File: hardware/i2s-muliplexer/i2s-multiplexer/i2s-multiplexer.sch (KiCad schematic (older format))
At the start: 18 parts, among them J1 Conn_01x07, J10 Conn_01x04, J2 Conn_01x04, J3 Conn_01x04, J4 Conn_01x04, J5 Conn_01x04, J6 Conn_01x04, J7 Conn_01x04, J8 Conn_01x04, J9 Conn_01x04, U1 74HC4051, U2 74HC4051, U3 74HC4051, U4 74HC4051, U5 74HC126

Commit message: Using buffers
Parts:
- removed J2, J7, J8, J9: Conn_01x04, Connector_PinHeader_2.54mm:PinHeader_1x04_P2.54mm_Vertical, symbol Connector_Generic:Conn_01x04
- removed U1, U2, U3, U4: 74HC4051, Package_SO:SOIC-16_3.9x9.9mm_P1.27mm, symbol 74xx:74HC4051
- removed U5: 74HC126, Package_SO:SOIC-14_3.9x8.7mm_P1.27mm, symbol 74xx:74LS126
- added J4: Conn_01x04, Connector_PinHeader_2.54mm:PinHeader_1x04_P2.54mm_Vertical, symbol Connector_Generic:Conn_01x04
- added R4, R6: 10K, symbol Device:R_Small
- added R5: R_Small, symbol Device:R_Small
- added U1, U2, U3, U4, U5, U6: 74HC126, symbol i2s-multiplexer:74HC126
- added U7: 74LS138, symbol 74xx:74LS138
- R1, R2, R3: footprint Resistor_SMD:R_0805_2012Metric_Pad1.15x1.40mm_HandSolder -> (none)
- renumbered J5 to J1, J4 to J2, J6 to J3, J3 to J5, J1 to J6, J10 to J7
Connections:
- net labels added: +3V3, CH_EN_0, CH_EN_1, CH_EN_2, CH_EN_3, CH_EN_4, SRC_EN
- net labels removed: BCLK_5, BCLK_6, BCLK_7, DATA_5, DATA_6, DATA_7, LRCLK_5, LRCLK_6, LRCLK_7, MCLK_5, MCLK_6, MCLK_7, ~SRC_EN
- wire segments 114 -> 172
- no-connect marks 0 -> 3
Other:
- note added: "BCLK"
- note added: "CD"
- note added: "CD\n"
- note added: "DAB \nRadio\n"
- note added: "DATA"
- note added: "LRCLK"
- note added: "MCLK_OUT"
- note added: "Media\nCenter\n"
- note added: "Record\nPlayer\n"
- note added: "SPDIF\nBlueray"
- note removed: "I2S Source Inputs\n"
- moved on the sheet: J6

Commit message: Initial PCB design
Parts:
- removed J7: Conn_01x04, Connector_PinHeader_2.54mm:PinHeader_1x04_P2.54mm_Vertical, symbol Connector_Generic:Conn_01x04
- added J7: Conn_01x05, Connector_PinHeader_2.54mm:PinHeader_1x05_P2.54mm_Vertical, symbol Connector_Generic:Conn_01x05
- J1, J2, J3, J4, J5: value Conn_01x04 -> Conn_01x05; footprint Connector_PinHeader_2.54mm:PinHeader_1x04_P2.54mm_Vertical -> Connector_PinHeader_2.54mm:PinHeader_1x05_P2.54mm_Vertical; symbol Connector_Generic:Conn_01x04 -> Connector_Generic:Conn_01x05
- R1, R2, R3, R4, R6: footprint (none) -> Resistor_SMD:R_0805_2012Metric_Pad1.15x1.40mm_HandSolder
- R5: value R_Small -> 10K; footprint (none) -> Resistor_SMD:R_0805_2012Metric_Pad1.15x1.40mm_HandSolder
- U1, U2, U3, U4, U5, U6: footprint (none) -> Package_SO:SOIC-14_3.9x8.7mm_P1.27mm
- U7: footprint (none) -> Package_SO:SOIC-16_3.9x9.9mm_P1.27mm
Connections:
- net labels added: BCLK_OUT, DATA_OUT, LRCLK_OUT, MCLK_OUT
- wire segments 172 -> 179
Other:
- note removed: "BCLK"
- note removed: "DATA"
- note removed: "LRCLK"
- note removed: "MCLK_OUT"
- moved on the sheet: R1, R2, R3, R4

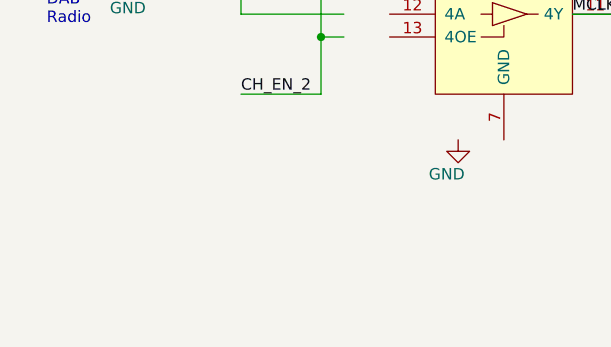
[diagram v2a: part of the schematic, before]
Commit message: Added test point
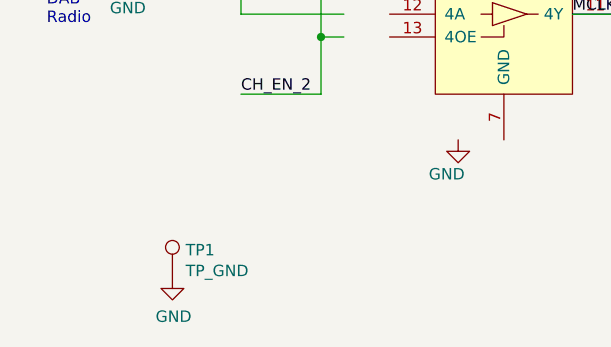
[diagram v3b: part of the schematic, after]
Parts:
- added TP1: TP_GND, Connector_PinHeader_2.54mm:PinHeader_1x01_P2.54mm_Vertical, symbol Connector:TestPoint
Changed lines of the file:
@@
 Text Label 10050 4800 0    50   ~ 0
 LRCLK_OUT
+$Comp
+L Connector:TestPoint TP1
+U 1 1 621031E6
+P 1400 7450
+F 0 "TP1" H 1458 7568 50  0000 L CNN
+F 1 "TP_GND" H 1458 7477 50  0000 L CNN
+F 2 "Connector_PinHeader_2.54mm:PinHeader_1x01_P2.54mm_Vertical" H 1600 7450 50  0001 C CNN
+F 3 "~" H 1600 7450 50  0001 C CNN
+	1    1400 7450
+	1    0    0    -1
+$EndComp
+$Comp
+L power:GND #PWR0105
+U 1 1 6210419F
+P 1400 7450
+F 0 "#PWR0105" H 1400 7200 50  0001 C CNN
+F 1 "GND" H 1405 7277 50  0000 C CNN
+F 2 "" H 1400 7450 50  0001 C CNN
+F 3 "" H 1400 7450 50  0001 C CNN
+	1    1400 7450
+	1    0    0    -1
+$EndComp
 $EndSCHEMATC

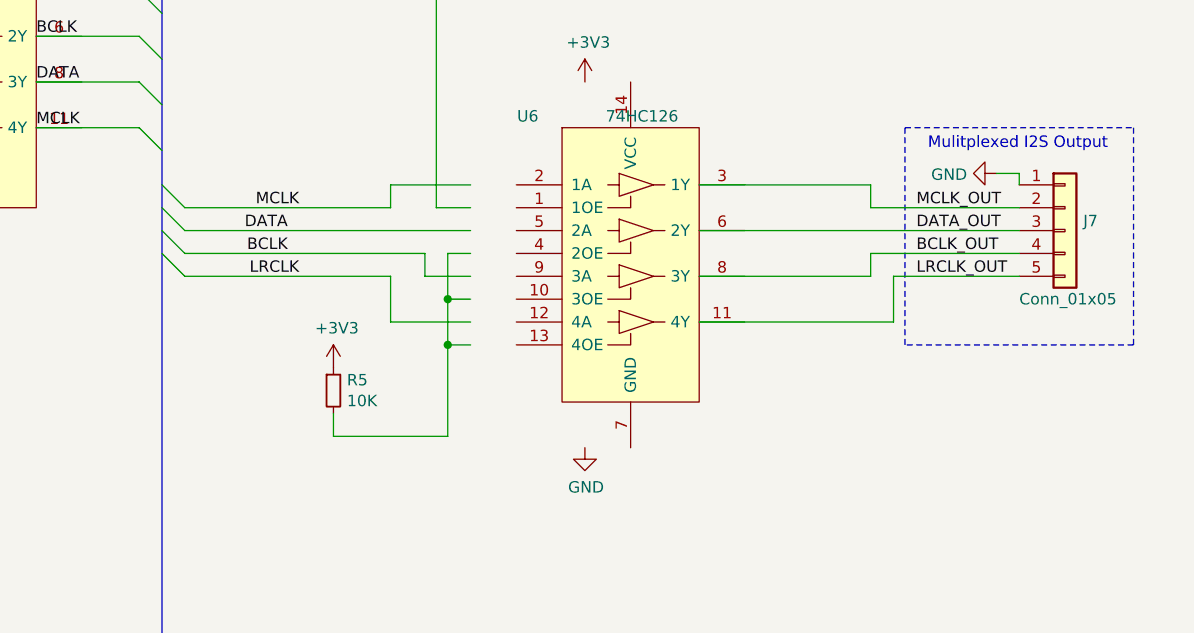
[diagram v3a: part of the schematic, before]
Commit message: Rationalised bus structure
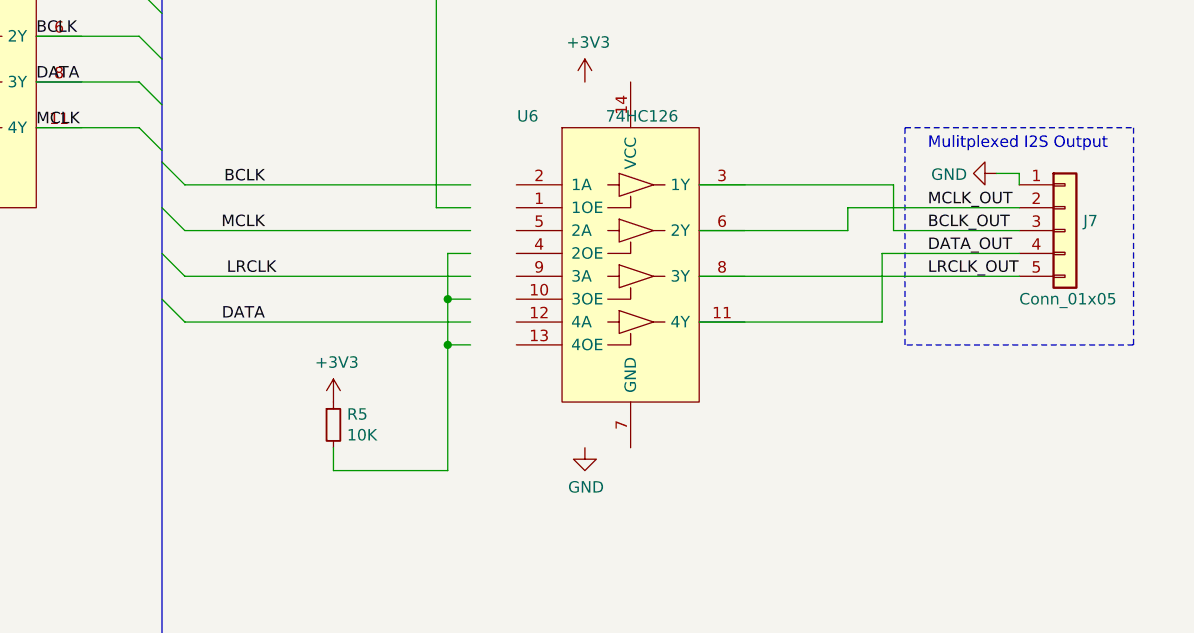
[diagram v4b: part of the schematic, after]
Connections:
- wire segments 179 -> 173
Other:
- moved on the sheet: R5
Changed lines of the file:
@@
 Comment4 ""
 $EndDescr
-Text Label 7350 4800 2    50   ~ 0
+Text Label 7250 4800 2    50   ~ 0
 LRCLK
-Text Label 7300 4700 2    50   ~ 0
+Text Label 7200 4400 2    50   ~ 0
 BCLK
-Text Label 7300 4600 2    50   ~ 0
+Text Label 7200 5000 2    50   ~ 0
 DATA
-Text Label 7350 4500 2    50   ~ 0
+Text Label 7200 4600 2    50   ~ 0
 MCLK
 $Comp
@@
 MCLK
 Entry Wire Line
-	6750 4400 6850 4500
+	6750 4300 6850 4400
 Entry Wire Line
 	6750 4500 6850 4600
 Entry Wire Line
-	6750 4600 6850 4700
+	6750 4900 6850 5000
 Entry Wire Line
 	6750 4700 6850 4800
@@
 	10000 4150 11000 4150
 Wire Wire Line
-	6850 4500 7750 4500
-Wire Wire Line
-	7750 4500 7750 4400
-Wire Wire Line
-	7750 4400 8100 4400
-Wire Wire Line
-	6850 4600 8100 4600
-Wire Wire Line
-	6850 4700 7900 4700
-Wire Wire Line
-	7900 4700 7900 4800
-Wire Wire Line
-	7900 4800 8100 4800
-Wire Wire Line
-	6850 4800 7750 4800
-Wire Wire Line
-	7750 4800 7750 5000
-Wire Wire Line
-	7750 5000 8100 5000
-Wire Wire Line
 	8800 1900 8800 2700
 Wire Wire Line
@@
 L Device:R_Small R5
 U 1 1 621C4F93
-P 7500 5300
-F 0 "R5" H 7559 5346 50  0000 L CNN
-F 1 "10K" H 7559 5255 50  0000 L CNN
-F 2 "Resistor_SMD:R_0805_2012Metric_Pad1.15x1.40mm_HandSolder" H 7500 5300 50  0001 C CNN
-F 3 "~" H 7500 5300 50  0001 C CNN
-	1    7500 5300
+P 7500 5450
+F 0 "R5" H 7559 5496 50  0000 L CNN
+F 1 "10K" H 7559 5405 50  0000 L CNN
+F 2 "Resistor_SMD:R_0805_2012Metric_Pad1.15x1.40mm_HandSolder" H 7500 5450 50  0001 C CNN
+F 3 "~" H 7500 5450 50  0001 C CNN
+	1    7500 5450
 	1    0    0    -1
 $EndComp
@@
 L power:+3V3 #PWR015
 U 1 1 621C5878
-P 7500 5200
-F 0 "#PWR015" H 7500 5050 50  0001 C CNN
-F 1 "+3V3" H 7515 5373 50  0000 C CNN
-F 2 "" H 7500 5200 50  0001 C CNN
-F 3 "" H 7500 5200 50  0001 C CNN
-	1    7500 5200
-	1    0    0    -1
-$EndComp
-Wire Wire Line
-	7500 5400 7500 5500
-Wire Wire Line
-	7500 5500 8000 5500
-Wire Wire Line
-	8000 5500 8000 5100
+P 7500 5350
+F 0 "#PWR015" H 7500 5200 50  0001 C CNN
+F 1 "+3V3" H 7515 5523 50  0000 C CNN
+F 2 "" H 7500 5350 50  0001 C CNN
+F 3 "" H 7500 5350 50  0001 C CNN
+	1    7500 5350
+	1    0    0    -1
+$EndComp
+Wire Wire Line
+	7500 5550 7500 5650
+Wire Wire Line
+	7500 5650 8000 5650
+Wire Wire Line
+	8000 5650 8000 5100
 Wire Wire Line
 	8000 4700 8100 4700
@@
 $EndComp
 Wire Wire Line
-	9100 4400 9850 4400
-Wire Wire Line
-	9850 4400 9850 4500
-Wire Wire Line
-	9850 4500 10500 4500
-Wire Wire Line
-	9100 4600 10500 4600
-Wire Wire Line
-	10500 4700 9850 4700
-Wire Wire Line
-	9850 4700 9850 4800
-Wire Wire Line
-	9850 4800 9100 4800
-Wire Wire Line
-	9100 5000 9950 5000
-Wire Wire Line
-	9950 5000 9950 4800
-Wire Wire Line
-	9950 4800 10500 4800
+	9100 5000 9900 5000
 Wire Wire Line
 	9400 1800 9400 2000
@@
 Wire Wire Line
 	10500 4350 10500 4400
-Wire Bus Line
-	3700 6550 6750 6550
-Wire Bus Line
-	3700 1250 3700 6550
-Wire Bus Line
-	6750 1250 6750 6550
-Text Label 10050 4500 0    50   ~ 0
+Text Label 10100 4500 0    50   ~ 0
 MCLK_OUT
-Text Label 10050 4600 0    50   ~ 0
+Text Label 10100 4700 0    50   ~ 0
 DATA_OUT
-Text Label 10050 4700 0    50   ~ 0
+Text Label 10100 4600 0    50   ~ 0
 BCLK_OUT
-Text Label 10050 4800 0    50   ~ 0
+Text Label 10100 4800 0    50   ~ 0
 LRCLK_OUT
 $Comp
@@
 	1    0    0    -1
 $EndComp
+Wire Wire Line
+	6850 4800 8100 4800
+Wire Wire Line
+	8100 5000 6850 5000
+Wire Wire Line
+	8100 4600 6850 4600
+Wire Wire Line
+	8100 4400 6850 4400
+Wire Wire Line
+	9100 4400 9950 4400
+Wire Wire Line
+	9950 4400 9950 4600
+Wire Wire Line
+	9950 4600 10500 4600
+Wire Wire Line
+	9100 4600 9750 4600
+Wire Wire Line
+	9750 4600 9750 4500
+Wire Wire Line
+	9750 4500 10500 4500
+Wire Wire Line
+	9100 4800 10500 4800
+Wire Wire Line
+	9900 5000 9900 4700
+Wire Wire Line
+	9900 4700 10500 4700
+Wire Bus Line
+	3700 6550 6750 6550
+Wire Bus Line
+	3700 1250 3700 6550
+Wire Bus Line
+	6750 1250 6750 6550
 $EndSCHEMATC

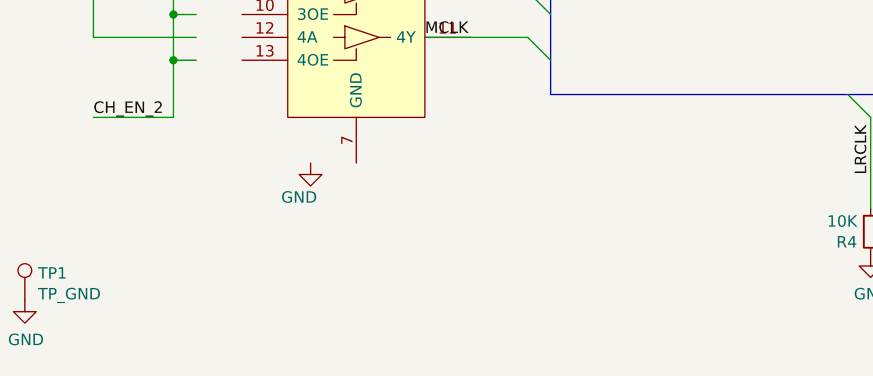
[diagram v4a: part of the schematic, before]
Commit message: Minor routing changes
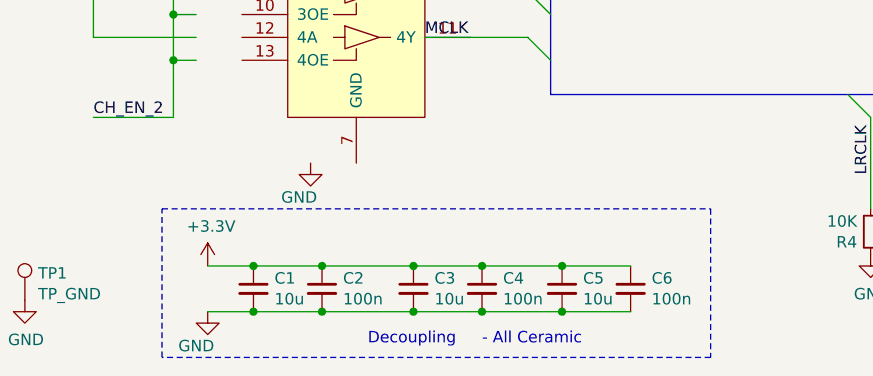
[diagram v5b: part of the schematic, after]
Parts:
- added C1, C3, C5: 10u, symbol Device:C_Small
- added C2, C4, C6: 100n, symbol Device:C_Small
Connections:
- wire segments 173 -> 185
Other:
- note added: "- All Ceramic"
- note added: "Decoupling"
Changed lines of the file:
@@
 Wire Wire Line
 	9900 4700 10500 4700
+$Comp
+L Device:C_Small C1
+U 1 1 61F53B6B
+P 2400 7400
+F 0 "C1" H 2492 7446 50  0000 L CNN
+F 1 "10u" H 2492 7355 50  0000 L CNN
+F 2 "" H 2400 7400 50  0001 C CNN
+F 3 "~" H 2400 7400 50  0001 C CNN
+	1    2400 7400
+	1    0    0    -1
+$EndComp
+$Comp
+L Device:C_Small C2
+U 1 1 61F53DD7
+P 2700 7400
+F 0 "C2" H 2792 7446 50  0000 L CNN
+F 1 "100n" H 2792 7355 50  0000 L CNN
+F 2 "" H 2700 7400 50  0001 C CNN
+F 3 "~" H 2700 7400 50  0001 C CNN
+	1    2700 7400
+	1    0    0    -1
+$EndComp
+$Comp
+L Device:C_Small C3
+U 1 1 61F55351
+P 3100 7400
+F 0 "C3" H 3192 7446 50  0000 L CNN
+F 1 "10u" H 3192 7355 50  0000 L CNN
+F 2 "" H 3100 7400 50  0001 C CNN
+F 3 "~" H 3100 7400 50  0001 C CNN
+	1    3100 7400
+	1    0    0    -1
+$EndComp
+$Comp
+L Device:C_Small C4
+U 1 1 61F55357
+P 3400 7400
+F 0 "C4" H 3492 7446 50  0000 L CNN
+F 1 "100n" H 3492 7355 50  0000 L CNN
+F 2 "" H 3400 7400 50  0001 C CNN
+F 3 "~" H 3400 7400 50  0001 C CNN
+	1    3400 7400
+	1    0    0    -1
+$EndComp
+$Comp
+L Device:C_Small C5
+U 1 1 61F5E748
+P 3750 7400
+F 0 "C5" H 3842 7446 50  0000 L CNN
+F 1 "10u" H 3842 7355 50  0000 L CNN
+F 2 "" H 3750 7400 50  0001 C CNN
+F 3 "~" H 3750 7400 50  0001 C CNN
+	1    3750 7400
+	1    0    0    -1
+$EndComp
+$Comp
+L Device:C_Small C6
+U 1 1 61F5E74E
+P 4050 7400
+F 0 "C6" H 4142 7446 50  0000 L CNN
+F 1 "100n" H 4142 7355 50  0000 L CNN
+F 2 "" H 4050 7400 50  0001 C CNN
+F 3 "~" H 4050 7400 50  0001 C CNN
+	1    4050 7400
+	1    0    0    -1
+$EndComp
+Wire Wire Line
+	2200 7300 2400 7300
+Connection ~ 2400 7300
+Wire Wire Line
+	2400 7300 2700 7300
+Connection ~ 2700 7300
+Wire Wire Line
+	2700 7300 3100 7300
+Connection ~ 3100 7300
+Wire Wire Line
+	3100 7300 3400 7300
+Connection ~ 3400 7300
+Wire Wire Line
+	3400 7300 3750 7300
+Connection ~ 3750 7300
+Wire Wire Line
+	3750 7300 4050 7300
+Wire Wire Line
+	2200 7500 2400 7500
+Connection ~ 2400 7500
+Wire Wire Line
+	2400 7500 2700 7500
+Connection ~ 2700 7500
+Wire Wire Line
+	2700 7500 3100 7500
+Connection ~ 3100 7500
+Wire Wire Line
+	3100 7500 3400 7500
+Connection ~ 3400 7500
+Wire Wire Line
+	3400 7500 3750 7500
+Connection ~ 3750 7500
+Wire Wire Line
+	3750 7500 4050 7500
+$Comp
+L power:GND #PWR0106
+U 1 1 61F7A23E
+P 2200 7500
+F 0 "#PWR0106" H 2200 7250 50  0001 C CNN
+F 1 "GND" H 2150 7350 50  0000 C CNN
+F 2 "" H 2200 7500 50  0001 C CNN
+F 3 "" H 2200 7500 50  0001 C CNN
+	1    2200 7500
+	1    0    0    -1
+$EndComp
+$Comp
+L power:+3.3V #PWR0113
+U 1 1 61F7A5E2
+P 2200 7300
+F 0 "#PWR0113" H 2200 7150 50  0001 C CNN
+F 1 "+3.3V" H 2215 7473 50  0000 C CNN
+F 2 "" H 2200 7300 50  0001 C CNN
+F 3 "" H 2200 7300 50  0001 C CNN
+	1    2200 7300
+	1    0    0    -1
+$EndComp
+Text Notes 2900 7650 0    50   ~ 0
+Decoupling
+Wire Notes Line
+	2000 7050 4400 7050
+Wire Notes Line
+	4400 7050 4400 7700
+Wire Notes Line
+	4400 7700 2000 7700
+Wire Notes Line
+	2000 7700 2000 7050
 Wire Bus Line
 	3700 6550 6750 6550
@@
 Wire Bus Line
 	6750 1250 6750 6550
+Text Notes 3400 7650 0    50   ~ 0
+- All Ceramic
 $EndSCHEMATC

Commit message: Initial placement
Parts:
- removed U1, U2, U3, U4, U5: 74HC126, Package_SO:SOIC-14_3.9x8.7mm_P1.27mm, symbol i2s-multiplexer:74HC126
- added C3, C7: 10u, Capacitor_SMD:C_0805_2012Metric_Pad1.15x1.40mm_HandSolder, symbol Device:C_Small
- added C5, C9: 100n, Capacitor_SMD:C_0805_2012Metric_Pad1.15x1.40mm_HandSolder, symbol Device:C_Small
- added J1: Conn_01x05, Connector_PinHeader_2.54mm:PinHeader_1x05_P2.54mm_Vertical, symbol Connector_Generic:Conn_01x05
- added R6: 10K, Resistor_SMD:R_0805_2012Metric_Pad1.15x1.40mm_HandSolder, symbol Device:R_Small
- added U1, U2, U3: 74HC244, Package_SO:SOIC-20W_7.5x12.8mm_P1.27mm, symbol 74xx:74HC244
- C1, C2: footprint (none) -> Capacitor_SMD:C_0805_2012Metric_Pad1.15x1.40mm_HandSolder
- C10: renamed from C6; footprint (none) -> Capacitor_SMD:C_0805_2012Metric_Pad1.15x1.40mm_HandSolder
- C4: renamed from C3; footprint (none) -> Capacitor_SMD:C_0805_2012Metric_Pad1.15x1.40mm_HandSolder
- C6: renamed from C4; footprint (none) -> Capacitor_SMD:C_0805_2012Metric_Pad1.15x1.40mm_HandSolder
- C8: renamed from C5; footprint (none) -> Capacitor_SMD:C_0805_2012Metric_Pad1.15x1.40mm_HandSolder
- renumbered J3 to J2, J1 to J3, J2 to J4, J4 to J6, J6 to J7, J7 to J8, R4 to R1, R3 to R2, R2 to R3, R1 to R4, R6 to R7, U6 to U4, U7 to U5
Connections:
- net labels added: A0, A1, A2, BCLK_5, CH_EN_5, DATA_5, LRCLK_5, MCLK_5
- net labels removed: S0, S1, S2
- wire segments 185 -> 94
- no-connect marks 3 -> 2
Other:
- note removed: "CD"
- moved on the sheet: C1, C10, C2, C4, C6, C8, J2, J3, J4, J5, J6, J7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
